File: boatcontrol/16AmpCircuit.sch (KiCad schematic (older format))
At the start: 5 parts, among them K6601 G5RL-K1A-E-DC12, Q6601 T9-818 16A, SW6601 ESB30, SW6602 ESB30

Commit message: Fix graphics
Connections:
- net OFF_COIL: now reaches K6601.8 (C8), SW6602.2 (B), SW6602.5 (B)
- net ON_COIL: now reaches K6601.1 (C1), SW6601.2 (B), SW6601.5 (B)
- net TO_FUSE: now reaches K6601.4 (NO), K6601.5 (NO), Q6601.P1 (P?)
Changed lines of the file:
@@
 Wire Wire Line
 	5250 4000 5250 4900
+Text Label 7350 3650 0    50   ~ 0
+TO_FUSE
+Text Label 6750 3550 0    50   ~ 0
+ON_COIL
+Text Label 6700 4500 0    50   ~ 0
+OFF_COIL
 $EndSCHEMATC

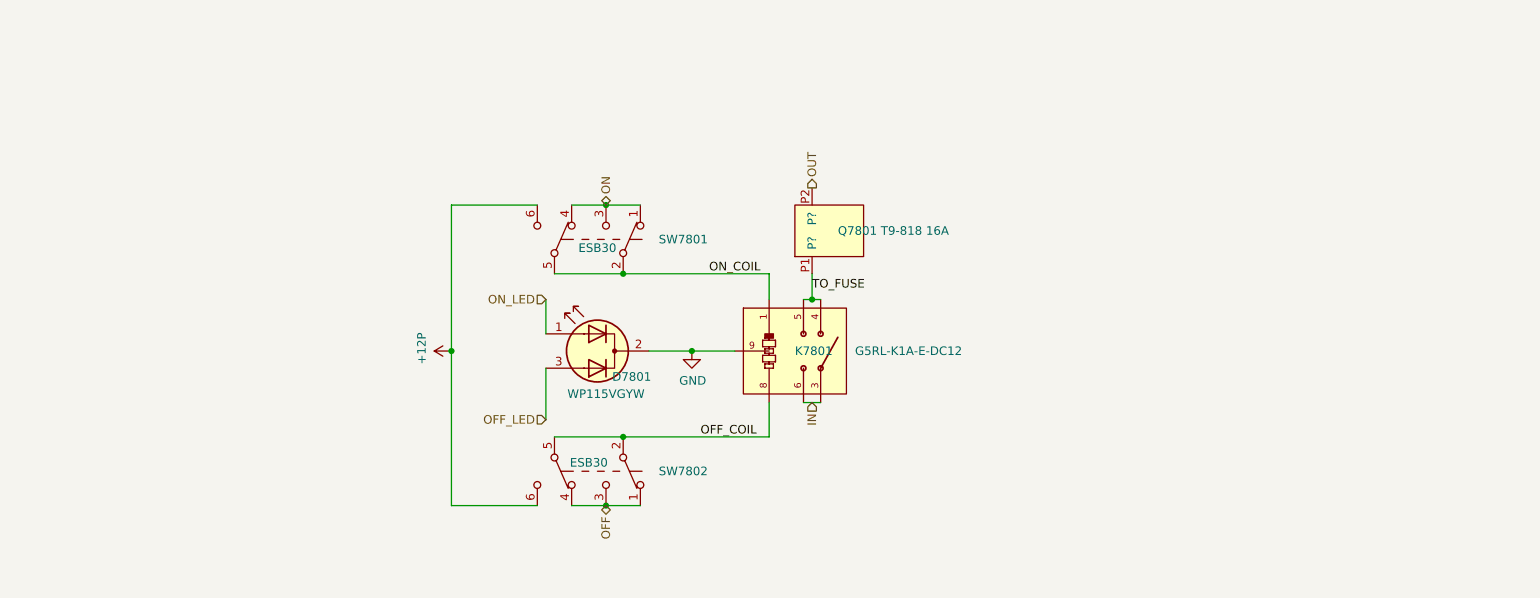
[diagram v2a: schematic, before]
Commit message: Fix switch layouts
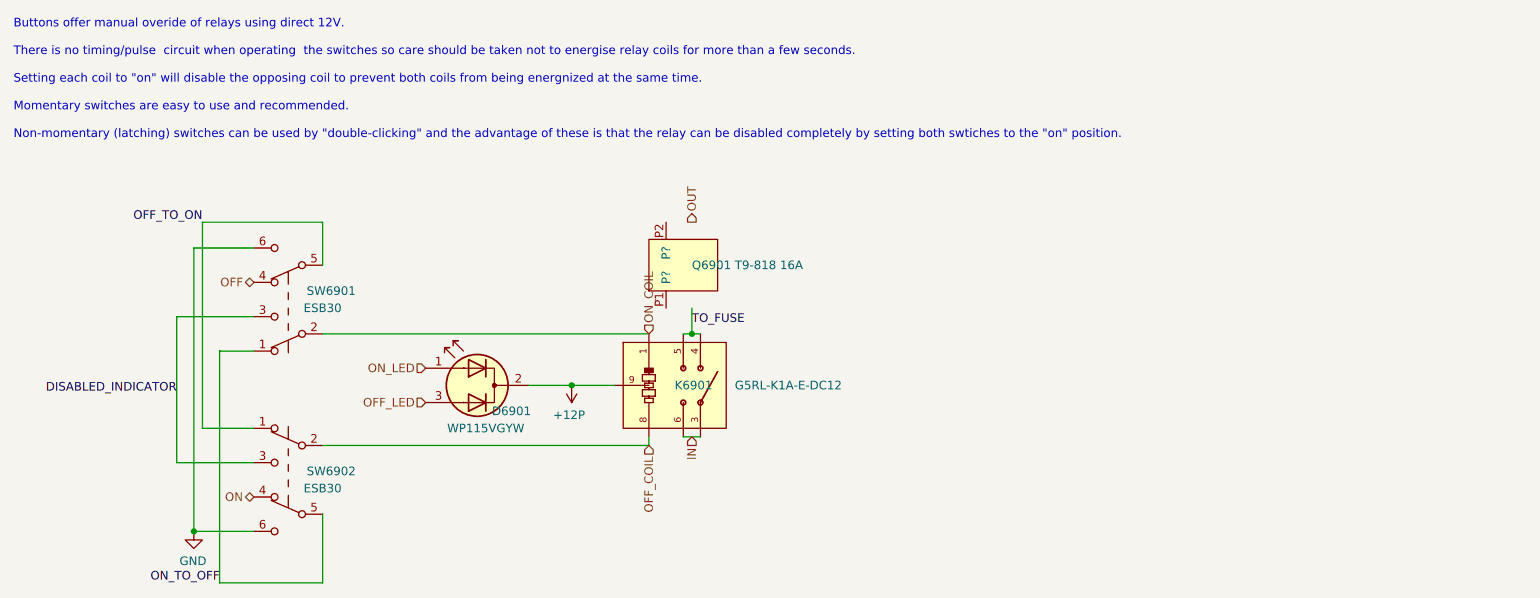
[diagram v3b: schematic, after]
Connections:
- net labels added: DISABLED_INDICATOR, OFF_TO_ON, ON_TO_OFF
- wire segments 22 -> 23
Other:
- note added: "Buttons offer manual overide of relays using direct 12V.\n\nThere is no timing/pulse circuit when operating the switches so care should be taken not to energise relay coils for more than a few seconds.\n\nSetting each coil to "on" will disable the opposing coil to prevent both coils from being energnized at the same time.\n\nMomentary switches are easy to use and recommended.\n\nNon-momentary (la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"
- moved on the sheet: D6901, K6901, Q6901, SW6901, SW6902

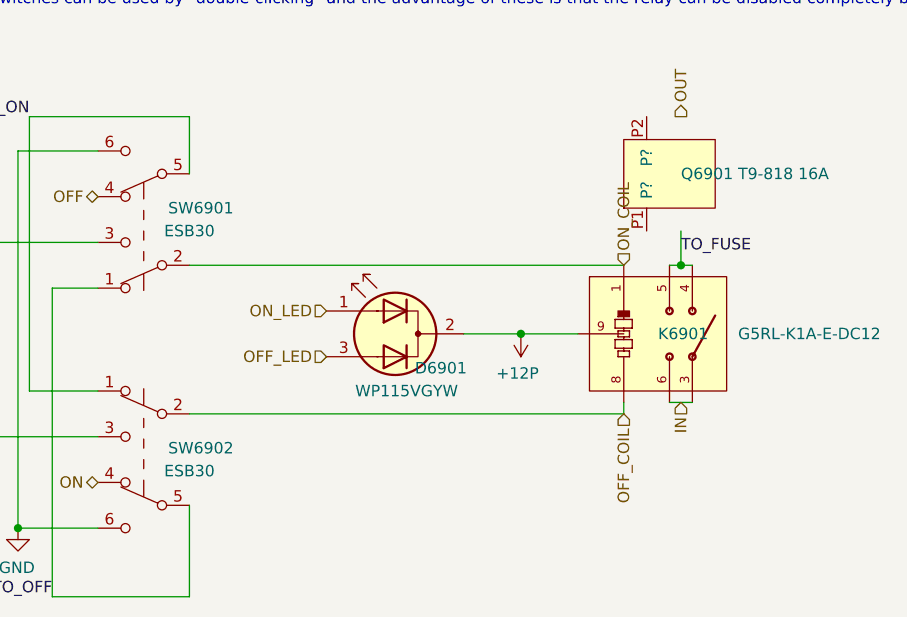
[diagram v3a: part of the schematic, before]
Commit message: Fix LED resistors
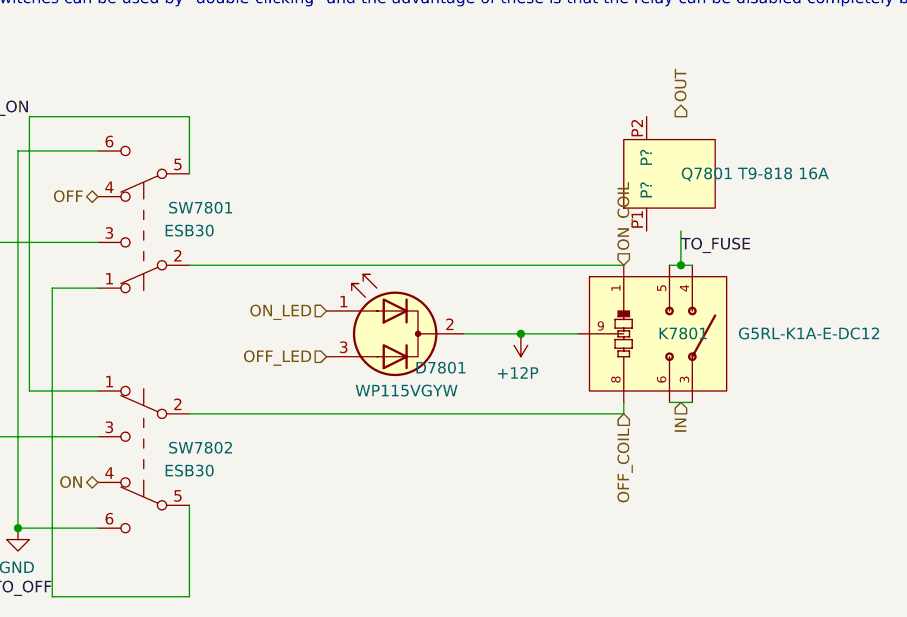
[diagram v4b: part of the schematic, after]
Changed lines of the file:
@@
 AR Path="/D1BB8DB4/5F75E923/604748F7/6123E075" Ref="D7501"  Part="1"
 AR Path="/D1BB8DB4/5F75E923/604748FF/6123E075" Ref="D7801"  Part="1"
-F 0 "D6901" H 5200 4050 50  0000 C CNN
+F 0 "D7801" H 5200 4050 50  0000 C CNN
 F 1 "WP115VGYW" H 5350 3950 50  0000 C CNN
 F 2 "LED_THT:LED_D5.0mm-3" H 5400 4200 50  0001 C CNN
@@
 AR Path="/D1BB8DB4/5F75E923/604748F7/E14E2028" Ref="K7501"  Part="1"
 AR Path="/D1BB8DB4/5F75E923/604748FF/E14E2028" Ref="K7801"  Part="1"
-F 0 "K6901" H 6550 4200 50  0000 L CNN
+F 0 "K7801" H 6550 4200 50  0000 L CNN
 F 1 "G5RL-K1A-E-DC12" H 6900 4200 50  0000 L CNN
 F 2 "RELAY_G5RL-K1A-E-DC12" H 6900 4350 50  0001 L BNN
@@
 AR Path="/D1BB8DB4/5F75E923/604748F7/E14E2029" Ref="Q7501"  Part="1"
 AR Path="/D1BB8DB4/5F75E923/604748FF/E14E2029" Ref="Q7801"  Part="1"
-F 0 "Q6901" V 6300 3150 50  0000 R CNN
+F 0 "Q7801" V 6300 3150 50  0000 R CNN
 F 1 "T9-818 16A" V 6300 2900 50  0000 R CNN
 F 2 "BoatControl:Schurter_Circuit_Breaker" H 6300 3500 50  0001 C CNN
@@
 AR Path="/D1BB8DB4/5F75E923/604748F7/E14E202A" Ref="SW7501"  Part="1"
 AR Path="/D1BB8DB4/5F75E923/604748FF/E14E202A" Ref="SW7801"  Part="1"
-F 0 "SW6901" H 4050 3650 50  0000 C CNN
+F 0 "SW7801" H 4050 3650 50  0000 C CNN
 F 1 " ESB30" H 4100 3750 50  0000 C CNN
 F 2 "BoatControl:SW_PUSH_ESB30_DPDT" H 4300 3900 50  0001 C CNN
@@
 AR Path="/D1BB8DB4/5F75E923/604748F7/62834852" Ref="SW7502"  Part="1"
 AR Path="/D1BB8DB4/5F75E923/604748FF/62834852" Ref="SW7802"  Part="1"
-F 0 "SW6902" H 4050 4800 50  0000 C CNN
+F 0 "SW7802" H 4050 4800 50  0000 C CNN
 F 1 " ESB30" H 4100 4700 50  0000 C CNN
 F 2 "BoatControl:SW_PUSH_ESB30_DPDT" H 4300 4950 50  0001 C CNN
@@
 AR Path="/D1BB8DB4/5F746103/60365C49/60DE8FA3" Ref="#PWR?"  Part="1"
 AR Path="/D1BB8DB4/5F746103/60365C53/60DE8FA3" Ref="#PWR?"  Part="1"
-AR Path="/D1BB8DB4/5F76AF55/604748F7/60DE8FA3" Ref="#PWR?"  Part="1"
-AR Path="/D1BB8DB4/5F76AF55/604748FF/60DE8FA3" Ref="#PWR?"  Part="1"
+AR Path="/D1BB8DB4/5F76AF55/604748F7/60DE8FA3" Ref="#PWR0131"  Part="1"
+AR Path="/D1BB8DB4/5F76AF55/604748FF/60DE8FA3" Ref="#PWR0137"  Part="1"
 AR Path="/D1BB8DB4/5F76AF55/60474907/60DE8FA3" Ref="#PWR?"  Part="1"
 AR Path="/D1BB8DB4/5F76AF55/60474911/60DE8FA3" Ref="#PWR?"  Part="1"
-AR Path="/D1BB8DB4/5F75E923/604748F7/60DE8FA3" Ref="#PWR?"  Part="1"
-AR Path="/D1BB8DB4/5F75E923/604748FF/60DE8FA3" Ref="#PWR?"  Part="1"
+AR Path="/D1BB8DB4/5F75E923/604748F7/60DE8FA3" Ref="#PWR0139"  Part="1"
+AR Path="/D1BB8DB4/5F75E923/604748FF/60DE8FA3" Ref="#PWR0145"  Part="1"
 AR Path="/D1BB8DB4/5F75E923/60474907/60DE8FA3" Ref="#PWR?"  Part="1"
 AR Path="/D1BB8DB4/5F75E923/60474911/60DE8FA3" Ref="#PWR?"  Part="1"
-F 0 "#PWR?" H 5950 4050 50  0001 C CNN
+F 0 "#PWR0145" H 5950 4050 50  0001 C CNN
 F 1 "+12P" H 5965 4373 50  0000 C CNN
 F 2 "" H 5950 4200 50  0001 C CNN
@@
 AR Path="/D1BB8DB4/5F746103/60365C49/60DE8FC4" Ref="#PWR?"  Part="1"
 AR Path="/D1BB8DB4/5F746103/60365C53/60DE8FC4" Ref="#PWR?"  Part="1"
-AR Path="/D1BB8DB4/5F76AF55/604748F7/60DE8FC4" Ref="#PWR?"  Part="1"
-AR Path="/D1BB8DB4/5F76AF55/604748FF/60DE8FC4" Ref="#PWR?"  Part="1"
+AR Path="/D1BB8DB4/5F76AF55/604748F7/60DE8FC4" Ref="#PWR0132"  Part="1"
+AR Path="/D1BB8DB4/5F76AF55/604748FF/60DE8FC4" Ref="#PWR0138"  Part="1"
 AR Path="/D1BB8DB4/5F76AF55/60474907/60DE8FC4" Ref="#PWR?"  Part="1"
 AR Path="/D1BB8DB4/5F76AF55/60474911/60DE8FC4" Ref="#PWR?"  Part="1"
-AR Path="/D1BB8DB4/5F75E923/604748F7/60DE8FC4" Ref="#PWR?"  Part="1"
-AR Path="/D1BB8DB4/5F75E923/604748FF/60DE8FC4" Ref="#PWR?"  Part="1"
+AR Path="/D1BB8DB4/5F75E923/604748F7/60DE8FC4" Ref="#PWR0140"  Part="1"
+AR Path="/D1BB8DB4/5F75E923/604748FF/60DE8FC4" Ref="#PWR0146"  Part="1"
 AR Path="/D1BB8DB4/5F75E923/60474907/60DE8FC4" Ref="#PWR?"  Part="1"
 AR Path="/D1BB8DB4/5F75E923/60474911/60DE8FC4" Ref="#PWR?"  Part="1"
-F 0 "#PWR?" H 3750 4800 50  0001 C CNN
+F 0 "#PWR0146" H 3750 4800 50  0001 C CNN
 F 1 "GND" H 3755 4877 50  0000 C CNN
 F 2 "" H 3750 5050 50  0001 C CNN

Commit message: Before re-order
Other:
- moved on the sheet: Q6901
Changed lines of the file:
@@
 AR Path="/D1BB8DB4/5F75E923/604748F7/6123E075" Ref="D7501"  Part="1"
 AR Path="/D1BB8DB4/5F75E923/604748FF/6123E075" Ref="D7801"  Part="1"
-F 0 "D7801" H 5200 4050 50  0000 C CNN
+F 0 "D6901" H 5200 4050 50  0000 C CNN
 F 1 "WP115VGYW" H 5350 3950 50  0000 C CNN
 F 2 "LED_THT:LED_D5.0mm-3" H 5400 4200 50  0001 C CNN
@@
 AR Path="/D1BB8DB4/5F75E923/604748F7/E14E2028" Ref="K7501"  Part="1"
 AR Path="/D1BB8DB4/5F75E923/604748FF/E14E2028" Ref="K7801"  Part="1"
-F 0 "K7801" H 6550 4200 50  0000 L CNN
+F 0 "K6901" H 6550 4200 50  0000 L CNN
 F 1 "G5RL-K1A-E-DC12" H 6900 4200 50  0000 L CNN
 F 2 "RELAY_G5RL-K1A-E-DC12" H 6900 4350 50  0001 L BNN
@@
 L BoatControl:SchurterCircuitBreaker Q?
 U 1 1 E14E2029
-P 6300 3500
+P 6450 3500
 AR Path="/E14E2029" Ref="Q?"  Part="1"
 AR Path="/5FBFBEC9/E14E2029" Ref="Q?"  Part="1"
@@
 AR Path="/D1BB8DB4/5F75E923/604748F7/E14E2029" Ref="Q7501"  Part="1"
 AR Path="/D1BB8DB4/5F75E923/604748FF/E14E2029" Ref="Q7801"  Part="1"
-F 0 "Q7801" V 6300 3150 50  0000 R CNN
-F 1 "T9-818 16A" V 6300 2900 50  0000 R CNN
-F 2 "BoatControl:Schurter_Circuit_Breaker" H 6300 3500 50  0001 C CNN
-F 3 "https://eu.mouser.com/datasheet/2/358/typ_T9-818-1276014.pdf" H 6300 3500 50  0001 C CNN
-F 4 "4404.0096" V 6300 3500 50  0001 C CNN "Manufacturer ID"
-	1    6300 3500
+F 0 "Q6901" V 6450 3150 50  0000 R CNN
+F 1 "T9-818 16A" V 6450 2900 50  0000 R CNN
+F 2 "BoatControl:Schurter_Circuit_Breaker" H 6450 3500 50  0001 C CNN
+F 3 "https://eu.mouser.com/datasheet/2/358/typ_T9-818-1276014.pdf" H 6450 3500 50  0001 C CNN
+F 4 "4404.0096" V 6450 3500 50  0001 C CNN "Manufacturer ID"
+	1    6450 3500
 	0    -1   -1   0
 $EndComp
@@
 AR Path="/D1BB8DB4/5F75E923/604748F7/E14E202A" Ref="SW7501"  Part="1"
 AR Path="/D1BB8DB4/5F75E923/604748FF/E14E202A" Ref="SW7801"  Part="1"
-F 0 "SW7801" H 4050 3650 50  0000 C CNN
+F 0 "SW6901" H 4050 3650 50  0000 C CNN
 F 1 " ESB30" H 4100 3750 50  0000 C CNN
 F 2 "BoatControl:SW_PUSH_ESB30_DPDT" H 4300 3900 50  0001 C CNN
@@
 AR Path="/D1BB8DB4/5F75E923/604748F7/62834852" Ref="SW7502"  Part="1"
 AR Path="/D1BB8DB4/5F75E923/604748FF/62834852" Ref="SW7802"  Part="1"
-F 0 "SW7802" H 4050 4800 50  0000 C CNN
+F 0 "SW6902" H 4050 4800 50  0000 C CNN
 F 1 " ESB30" H 4100 4700 50  0000 C CNN
 F 2 "BoatControl:SW_PUSH_ESB30_DPDT" H 4300 4950 50  0001 C CNN
@@
 AR Path="/D1BB8DB4/5F75E923/60474907/60DE8FA3" Ref="#PWR?"  Part="1"
 AR Path="/D1BB8DB4/5F75E923/60474911/60DE8FA3" Ref="#PWR?"  Part="1"
-F 0 "#PWR0145" H 5950 4050 50  0001 C CNN
+F 0 "#PWR0137" H 5950 4050 50  0001 C CNN
 F 1 "+12P" H 5965 4373 50  0000 C CNN
 F 2 "" H 5950 4200 50  0001 C CNN
@@
 AR Path="/D1BB8DB4/5F75E923/60474907/60DE8FC4" Ref="#PWR?"  Part="1"
 AR Path="/D1BB8DB4/5F75E923/60474911/60DE8FC4" Ref="#PWR?"  Part="1"
-F 0 "#PWR0146" H 3750 4800 50  0001 C CNN
+F 0 "#PWR0138" H 3750 4800 50  0001 C CNN
 F 1 "GND" H 3755 4877 50  0000 C CNN
 F 2 "" H 3750 5050 50  0001 C CNN

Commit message: Move In
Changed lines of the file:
@@
 $Descr A4 11693 8268
 encoding utf-8
-Sheet 69 87
+Sheet 66 87
 Title "Boat Control Hat"
 Date "2020-07-09"
@@
 AR Path="/D1BB8DB4/5F75E923/604748F7/6123E075" Ref="D7501"  Part="1"
 AR Path="/D1BB8DB4/5F75E923/604748FF/6123E075" Ref="D7801"  Part="1"
-F 0 "D6901" H 5200 4050 50  0000 C CNN
+F 0 "D6601" H 5200 4050 50  0000 C CNN
 F 1 "WP115VGYW" H 5350 3950 50  0000 C CNN
 F 2 "LED_THT:LED_D5.0mm-3" H 5400 4200 50  0001 C CNN
@@
 AR Path="/D1BB8DB4/5F75E923/604748F7/E14E2028" Ref="K7501"  Part="1"
 AR Path="/D1BB8DB4/5F75E923/604748FF/E14E2028" Ref="K7801"  Part="1"
-F 0 "K6901" H 6550 4200 50  0000 L CNN
+F 0 "K6601" H 6550 4200 50  0000 L CNN
 F 1 "G5RL-K1A-E-DC12" H 6900 4200 50  0000 L CNN
 F 2 "RELAY_G5RL-K1A-E-DC12" H 6900 4350 50  0001 L BNN
@@
 AR Path="/D1BB8DB4/5F75E923/604748F7/E14E2029" Ref="Q7501"  Part="1"
 AR Path="/D1BB8DB4/5F75E923/604748FF/E14E2029" Ref="Q7801"  Part="1"
-F 0 "Q6901" V 6450 3150 50  0000 R CNN
+F 0 "Q6601" V 6450 3150 50  0000 R CNN
 F 1 "T9-818 16A" V 6450 2900 50  0000 R CNN
 F 2 "BoatControl:Schurter_Circuit_Breaker" H 6450 3500 50  0001 C CNN
@@
 AR Path="/D1BB8DB4/5F75E923/604748F7/E14E202A" Ref="SW7501"  Part="1"
 AR Path="/D1BB8DB4/5F75E923/604748FF/E14E202A" Ref="SW7801"  Part="1"
-F 0 "SW6901" H 4050 3650 50  0000 C CNN
+F 0 "SW6601" H 4050 3650 50  0000 C CNN
 F 1 " ESB30" H 4100 3750 50  0000 C CNN
 F 2 "BoatControl:SW_PUSH_ESB30_DPDT" H 4300 3900 50  0001 C CNN
@@
 AR Path="/D1BB8DB4/5F75E923/604748F7/62834852" Ref="SW7502"  Part="1"
 AR Path="/D1BB8DB4/5F75E923/604748FF/62834852" Ref="SW7802"  Part="1"
-F 0 "SW6902" H 4050 4800 50  0000 C CNN
+F 0 "SW6602" H 4050 4800 50  0000 C CNN
 F 1 " ESB30" H 4100 4700 50  0000 C CNN
 F 2 "BoatControl:SW_PUSH_ESB30_DPDT" H 4300 4950 50  0001 C CNN
@@
 AR Path="/D1BB8DB4/5F75E923/60474907/60DE8FA3" Ref="#PWR?"  Part="1"
 AR Path="/D1BB8DB4/5F75E923/60474911/60DE8FA3" Ref="#PWR?"  Part="1"
-F 0 "#PWR0137" H 5950 4050 50  0001 C CNN
+F 0 "#PWR0139" H 5950 4050 50  0001 C CNN
 F 1 "+12P" H 5965 4373 50  0000 C CNN
 F 2 "" H 5950 4200 50  0001 C CNN
@@
 AR Path="/D1BB8DB4/5F75E923/60474907/60DE8FC4" Ref="#PWR?"  Part="1"
 AR Path="/D1BB8DB4/5F75E923/60474911/60DE8FC4" Ref="#PWR?"  Part="1"
-F 0 "#PWR0138" H 3750 4800 50  0001 C CNN
+F 0 "#PWR0140" H 3750 4800 50  0001 C CNN
 F 1 "GND" H 3755 4877 50  0000 C CNN
 F 2 "" H 3750 5050 50  0001 C CNN

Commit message: Figure out wiring cluster
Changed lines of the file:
@@
 $Descr A4 11693 8268
 encoding utf-8
-Sheet 66 87
+Sheet 67 87
 Title "Boat Control Hat"
 Date "2020-07-09"
@@
 AR Path="/D1BB8DB4/5F75E923/604748F7/6123E075" Ref="D7501"  Part="1"
 AR Path="/D1BB8DB4/5F75E923/604748FF/6123E075" Ref="D7801"  Part="1"
-F 0 "D6601" H 5200 4050 50  0000 C CNN
+F 0 "D6901" H 5200 4050 50  0000 C CNN
 F 1 "WP115VGYW" H 5350 3950 50  0000 C CNN
 F 2 "LED_THT:LED_D5.0mm-3" H 5400 4200 50  0001 C CNN
@@
 AR Path="/D1BB8DB4/5F75E923/604748F7/E14E2028" Ref="K7501"  Part="1"
 AR Path="/D1BB8DB4/5F75E923/604748FF/E14E2028" Ref="K7801"  Part="1"
-F 0 "K6601" H 6550 4200 50  0000 L CNN
+F 0 "K6901" H 6550 4200 50  0000 L CNN
 F 1 "G5RL-K1A-E-DC12" H 6900 4200 50  0000 L CNN
 F 2 "RELAY_G5RL-K1A-E-DC12" H 6900 4350 50  0001 L BNN
@@
 AR Path="/D1BB8DB4/5F75E923/604748F7/E14E2029" Ref="Q7501"  Part="1"
 AR Path="/D1BB8DB4/5F75E923/604748FF/E14E2029" Ref="Q7801"  Part="1"
-F 0 "Q6601" V 6450 3150 50  0000 R CNN
+F 0 "Q6901" V 6450 3150 50  0000 R CNN
 F 1 "T9-818 16A" V 6450 2900 50  0000 R CNN
 F 2 "BoatControl:Schurter_Circuit_Breaker" H 6450 3500 50  0001 C CNN
@@
 AR Path="/D1BB8DB4/5F75E923/604748F7/E14E202A" Ref="SW7501"  Part="1"
 AR Path="/D1BB8DB4/5F75E923/604748FF/E14E202A" Ref="SW7801"  Part="1"
-F 0 "SW6601" H 4050 3650 50  0000 C CNN
+F 0 "SW6901" H 4050 3650 50  0000 C CNN
 F 1 " ESB30" H 4100 3750 50  0000 C CNN
 F 2 "BoatControl:SW_PUSH_ESB30_DPDT" H 4300 3900 50  0001 C CNN
@@
 AR Path="/D1BB8DB4/5F75E923/604748F7/62834852" Ref="SW7502"  Part="1"
 AR Path="/D1BB8DB4/5F75E923/604748FF/62834852" Ref="SW7802"  Part="1"
-F 0 "SW6602" H 4050 4800 50  0000 C CNN
+F 0 "SW6902" H 4050 4800 50  0000 C CNN
 F 1 " ESB30" H 4100 4700 50  0000 C CNN
 F 2 "BoatControl:SW_PUSH_ESB30_DPDT" H 4300 4950 50  0001 C CNN

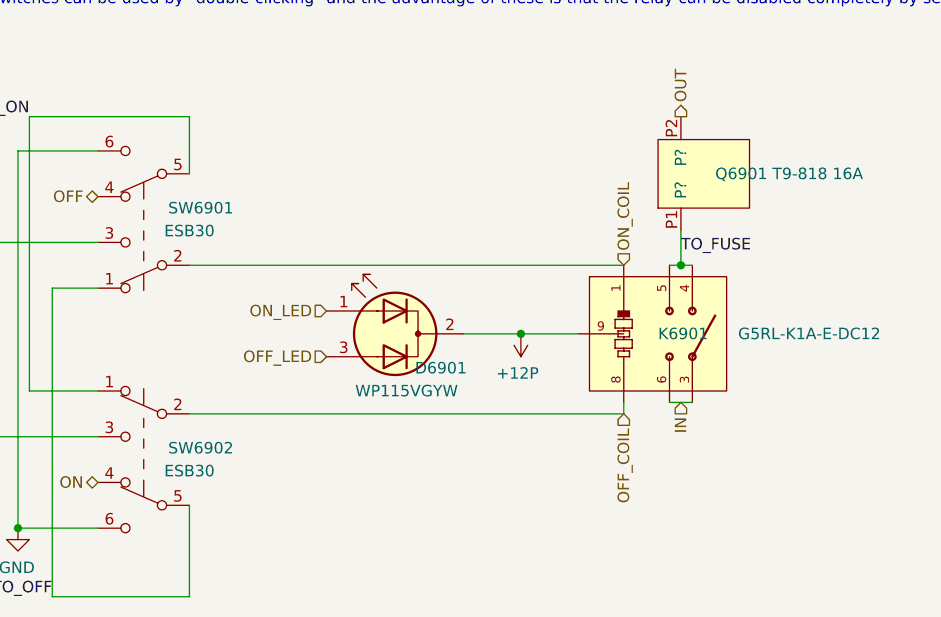
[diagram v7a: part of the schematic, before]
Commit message: Add remaining bypass capacitors
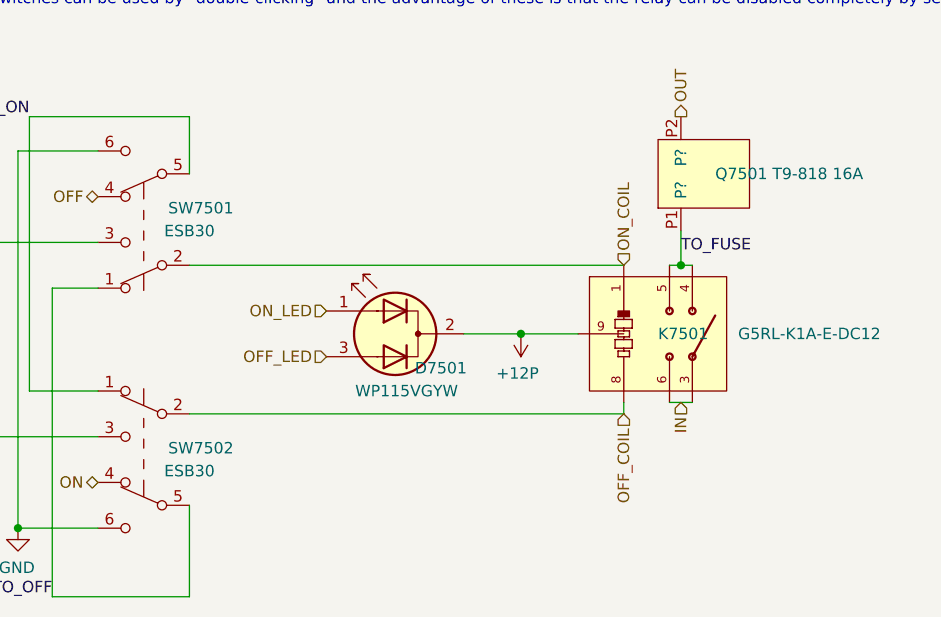
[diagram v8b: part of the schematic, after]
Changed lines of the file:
@@
 AR Path="/D1BB8DB4/5F75E923/604748F7/6123E075" Ref="D7501"  Part="1"
 AR Path="/D1BB8DB4/5F75E923/604748FF/6123E075" Ref="D7801"  Part="1"
-F 0 "D6901" H 5200 4050 50  0000 C CNN
+F 0 "D7501" H 5200 4050 50  0000 C CNN
 F 1 "WP115VGYW" H 5350 3950 50  0000 C CNN
 F 2 "LED_THT:LED_D5.0mm-3" H 5400 4200 50  0001 C CNN
@@
 AR Path="/D1BB8DB4/5F75E923/604748F7/E14E2028" Ref="K7501"  Part="1"
 AR Path="/D1BB8DB4/5F75E923/604748FF/E14E2028" Ref="K7801"  Part="1"
-F 0 "K6901" H 6550 4200 50  0000 L CNN
+F 0 "K7501" H 6550 4200 50  0000 L CNN
 F 1 "G5RL-K1A-E-DC12" H 6900 4200 50  0000 L CNN
 F 2 "RELAY_G5RL-K1A-E-DC12" H 6900 4350 50  0001 L BNN
@@
 AR Path="/D1BB8DB4/5F75E923/604748F7/E14E2029" Ref="Q7501"  Part="1"
 AR Path="/D1BB8DB4/5F75E923/604748FF/E14E2029" Ref="Q7801"  Part="1"
-F 0 "Q6901" V 6450 3150 50  0000 R CNN
+F 0 "Q7501" V 6450 3150 50  0000 R CNN
 F 1 "T9-818 16A" V 6450 2900 50  0000 R CNN
 F 2 "BoatControl:Schurter_Circuit_Breaker" H 6450 3500 50  0001 C CNN
@@
 AR Path="/D1BB8DB4/5F75E923/604748F7/E14E202A" Ref="SW7501"  Part="1"
 AR Path="/D1BB8DB4/5F75E923/604748FF/E14E202A" Ref="SW7801"  Part="1"
-F 0 "SW6901" H 4050 3650 50  0000 C CNN
+F 0 "SW7501" H 4050 3650 50  0000 C CNN
 F 1 " ESB30" H 4100 3750 50  0000 C CNN
 F 2 "BoatControl:SW_PUSH_ESB30_DPDT" H 4300 3900 50  0001 C CNN
@@
 AR Path="/D1BB8DB4/5F75E923/604748F7/62834852" Ref="SW7502"  Part="1"
 AR Path="/D1BB8DB4/5F75E923/604748FF/62834852" Ref="SW7802"  Part="1"
-F 0 "SW6902" H 4050 4800 50  0000 C CNN
+F 0 "SW7502" H 4050 4800 50  0000 C CNN
 F 1 " ESB30" H 4100 4700 50  0000 C CNN
 F 2 "BoatControl:SW_PUSH_ESB30_DPDT" H 4300 4950 50  0001 C CNN
